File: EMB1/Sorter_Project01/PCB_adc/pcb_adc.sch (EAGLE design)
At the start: 10 parts, among them IC1 LM358N, K2 61201021621

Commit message: new boards
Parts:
- removed BLUE1, BLUE2, GREEN1, GREEN2, OPTO, RED1, RED2: (no value), led:LED5MM
- removed IC1: LM358N, linear:LM358N
- removed K2: 61201021621, Wurth_Elektronik_Electromechanic_Wire_to_Board_Connectors_rev15c:61201021621
- added K1: 61201021621, Wurth_Elektronik_Electromechanic_Wire_to_Board_Connectors_rev15c:61201021621
- added Q1, Q2, Q3: IRF512, transistor-power:IRF512
- added R2, R3, R8, R9: 1K, resistor:R-US_0204/7
- added R4, R5, R6: 100K, resistor:R-US_0204/7
- added R7: 430, resistor:R-US_0204/7
- added SL1: (no value), con-amp-quick:M12
- added U$1: MCP3008P, MCP3008:MCP3008P
- R1: value (none) -> 1K; device resistor:R-EU_0207/10 -> resistor:R-US_0204/7
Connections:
- removed net 12V: BLUE1.A, BLUE2.A, GREEN1.A, GREEN2.A, K2.1, RED1.A, RED2.A
- removed net 5V: IC1P.V+, K2.10
- removed net BLUE: BLUE1.C, BLUE2.C, K2.5
- removed net GREEN: GREEN1.C, GREEN2.C, K2.3
- removed net PHD: IC1A.OUT, K2.8, R1.2
- removed net RED: K2.7, RED1.C, RED2.C
- new net +12V: K1.1, SL1.12
- new net +5V: K1.10, SL1.9, U$1.VDD, U$1.VREF
- new net CLK: SL1.7, U$1.SCK
- new net CS: SL1.4, U$1.!CS
- new net C_BLUE: R3.1, SL1.1
- new net C_GREEN: R2.1, SL1.3
- new net C_RED: R1.1, SL1.2
- new net MISO: SL1.6, U$1.MISO
- new net MOSI: SL1.5, U$1.MOSI
- new net N$1: Q1.G, R1.2, R4.2
- new net N$3: Q3.G, R3.2, R6.2
- new net N$4: Q1.D, R7.1
- new net N$5: Q2.D, R8.1
- new net N$8: Q3.D, R9.1
- new net OPTO: K1.8, U$1.CH0
- new net V_BLUE: K1.5, R9.2
- new net V_GREEN: K1.3, R8.2
- new net V_RED: K1.7, R7.2
- net GND: now also K1.2, K1.4, K1.6, K1.9, Q1.S, Q2.S, Q3.S, R4.1, R5.1, R6.1, SL1.10, SL1.11, SL1.8, U$1.AGND, U$1.CH1, U$1.CH2, U$1.CH3, U$1.CH4, U$1.CH5, U$1.CH6, U$1.CH7, U$1.GND; no longer IC1A.-IN, IC1B.+IN, IC1B.-IN, IC1B.OUT, IC1P.V-, K2.2, K2.4, K2.6, K2.9, OPTO.A
- net N$2: now also Q2.G, R2.2, R5.2; no longer IC1A.+IN, OPTO.C, R1.1

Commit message: report images added
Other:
- moved on the sheet: K1, Q1, Q2, Q3, R1, R2, R3, R4, R5, R6, R7, R8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

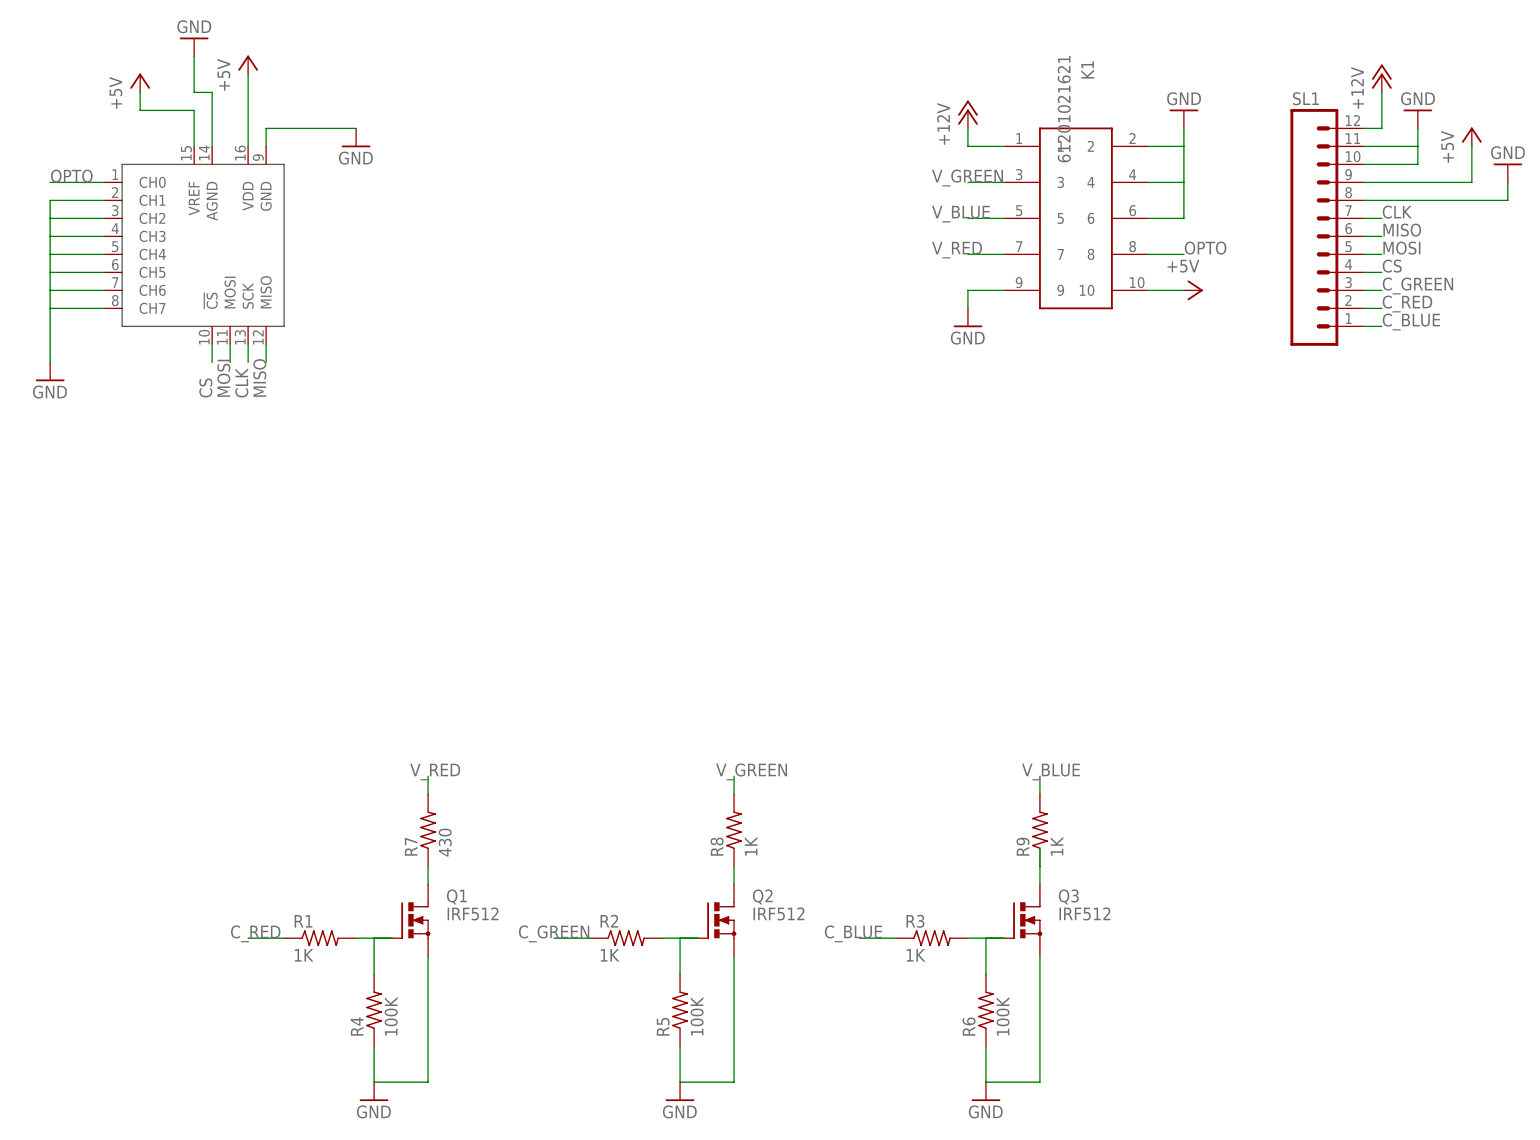
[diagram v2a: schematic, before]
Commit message: VHDL updated, now the blinking works due to bug pulsing data-updated for too long
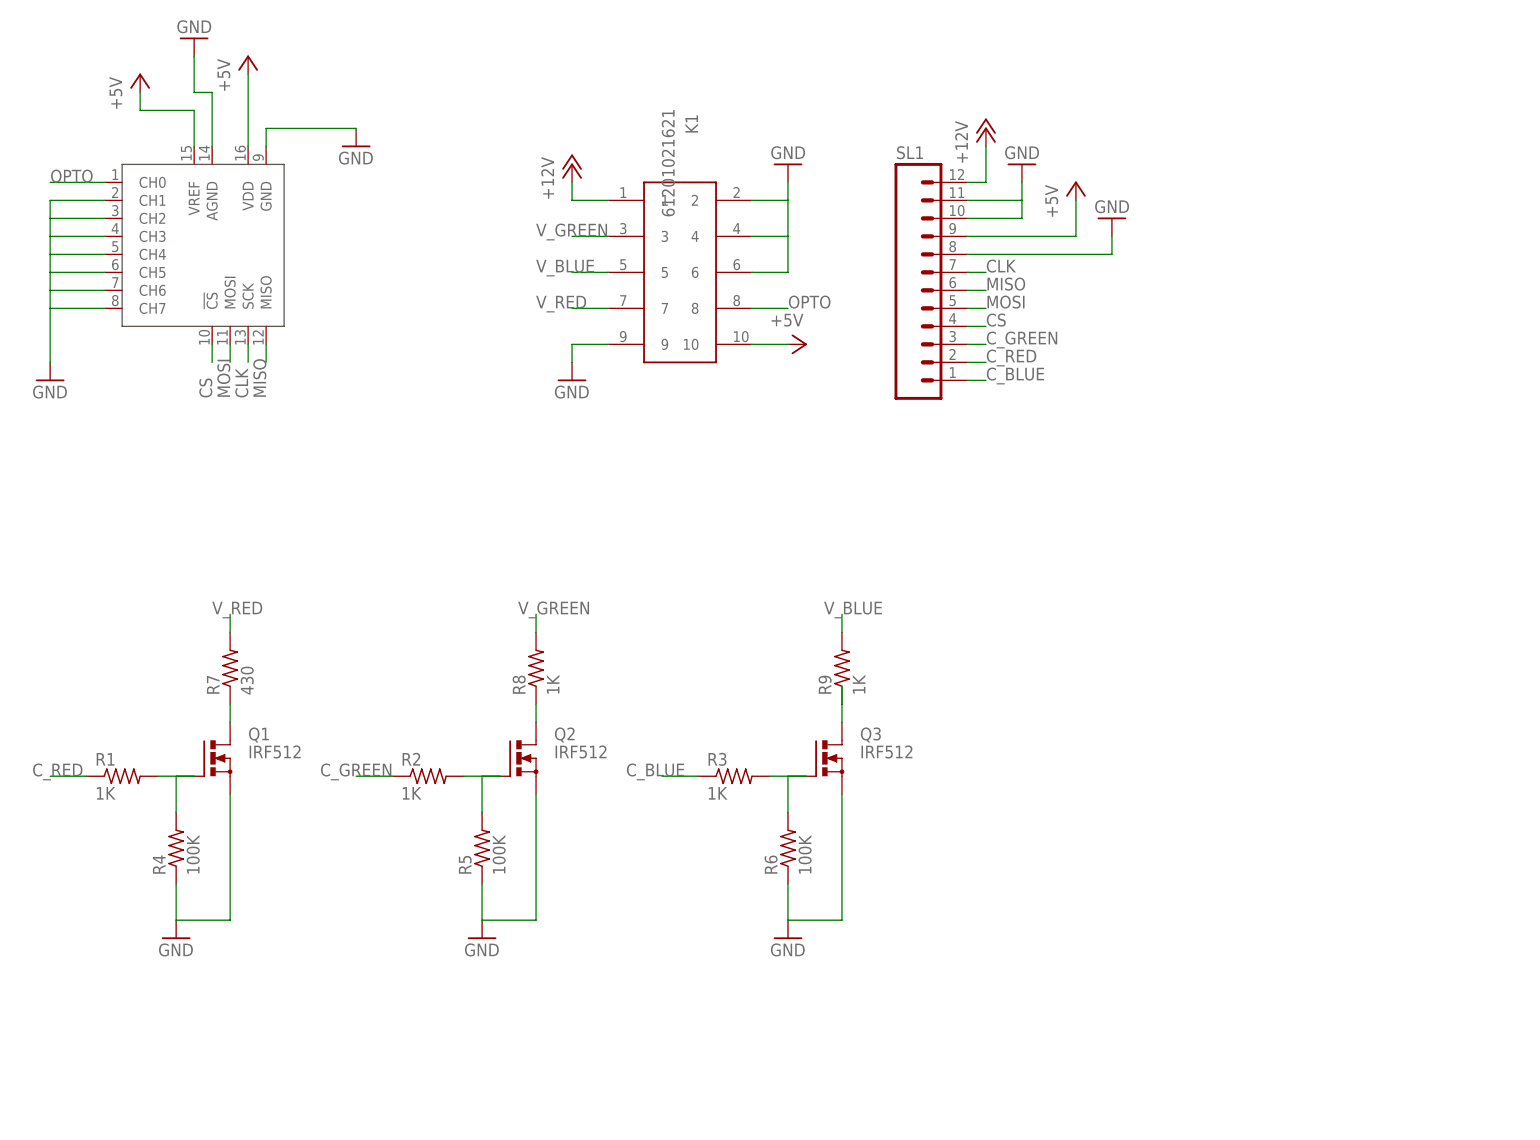
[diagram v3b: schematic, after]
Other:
- moved on the sheet: K1, Q1, Q2, Q3, R1, R2, R3, R4, R5, R6, R7, R8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

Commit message: report updated
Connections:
- new net +3V3: SL1.9, U$1.VDD, U$1.VREF
- net +5V: no longer SL1.9, U$1.VDD, U$1.VREF
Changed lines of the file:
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@@
 <part name="GND5" library="supply1" deviceset="GND" device=""/>
 <part name="GND6" library="supply1" deviceset="GND" device=""/>
-<part name="P+1" library="supply1" deviceset="+5V" device=""/>
-<part name="P+2" library="supply1" deviceset="+5V" device=""/>
 <part name="P+3" library="supply1" deviceset="+5V" device=""/>
 <part name="GND8" library="supply1" deviceset="GND" device=""/>
@@
 <part name="R8" library="resistor" deviceset="R-US_" device="0204/7" value="1K"/>
 <part name="R9" library="resistor" deviceset="R-US_" device="0204/7" value="1K"/>
-<part name="P+4" library="supply1" deviceset="+5V" device=""/>
 <part name="P+5" library="supply1" deviceset="+12V" device=""/>
 <part name="GND9" library="supply1" deviceset="GND" device=""/>
@@
 <part name="GND11" library="supply1" deviceset="GND" device=""/>
 <part name="P+7" library="supply1" deviceset="+12V" device=""/>
+<part name="+3V1" library="supply1" deviceset="+3V3" device=""/>
+<part name="+3V2" library="supply1" deviceset="+3V3" device=""/>
+<part name="+3V3" library="supply1" deviceset="+3V3" device=""/>
+<part name="+3V4" library="supply1" deviceset="+3V3" device=""/>
 </parts>
 <sheets>
@@
 <instance part="GND5" gate="1" x="7.62" y="99.06"/>
 <instance part="GND6" gate="1" x="38.1" y="66.04"/>
-<instance part="P+1" gate="1" x="-22.86" y="109.22"/>
-<instance part="P+2" gate="1" x="-7.62" y="111.76"/>
 <instance part="P+3" gate="1" x="71.12" y="71.12" rot="R270"/>
 <instance part="GND8" gate="1" x="-15.24" y="114.3" rot="R180"/>
@@
 <instance part="R8" gate="G$1" x="33.02" y="25.4" rot="R90"/>
 <instance part="R9" gate="G$1" x="76.2" y="25.4" rot="R90"/>
-<instance part="P+4" gate="1" x="109.22" y="93.98"/>
 <instance part="P+5" gate="1" x="96.52" y="101.6"/>
 <instance part="GND9" gate="1" x="114.3" y="88.9" rot="R180"/>
@@
 <instance part="GND11" gate="1" x="68.58" y="96.52" rot="R180"/>
 <instance part="P+7" gate="1" x="38.1" y="96.52"/>
+<instance part="+3V1" gate="G$1" x="-7.62" y="111.76"/>
+<instance part="+3V2" gate="G$1" x="-22.86" y="109.22"/>
+<instance part="+3V3" gate="G$1" x="76.2" y="73.66"/>
+<instance part="+3V4" gate="G$1" x="109.22" y="93.98"/>
 </instances>
 <busses>
@@
 <net name="+5V" class="0">
 <segment>
-<pinref part="U$1" gate="G$1" pin="VREF"/>
-<wire x1="-15.24" y1="99.06" x2="-15.24" y2="104.14" width="0.1524" layer="91"/>
-<wire x1="-15.24" y1="104.14" x2="-22.86" y2="104.14" width="0.1524" layer="91"/>
-<pinref part="P+1" gate="1" pin="+5V"/>
-<wire x1="-22.86" y1="104.14" x2="-22.86" y2="106.68" width="0.1524" layer="91"/>
-</segment>
-<segment>
-<pinref part="U$1" gate="G$1" pin="VDD"/>
-<pinref part="P+2" gate="1" pin="+5V"/>
-<wire x1="-7.62" y1="99.06" x2="-7.62" y2="109.22" width="0.1524" layer="91"/>
-</segment>
-<segment>
-<pinref part="P+4" gate="1" pin="+5V"/>
-<pinref part="SL1" gate="G$1" pin="9"/>
-<wire x1="93.98" y1="86.36" x2="109.22" y2="86.36" width="0.1524" layer="91"/>
-<wire x1="109.22" y1="86.36" x2="109.22" y2="91.44" width="0.1524" layer="91"/>
-</segment>
-<segment>
 <pinref part="K1" gate="G$1" pin="10"/>
 <pinref part="P+3" gate="1" pin="+5V"/>
@@
 </segment>
 </net>
+<net name="+3V3" class="0">
+<segment>
+<pinref part="U$1" gate="G$1" pin="VREF"/>
+<wire x1="-15.24" y1="99.06" x2="-15.24" y2="104.14" width="0.1524" layer="91"/>
+<wire x1="-15.24" y1="104.14" x2="-22.86" y2="104.14" width="0.1524" layer="91"/>
+<wire x1="-22.86" y1="104.14" x2="-22.86" y2="106.68" width="0.1524" layer="91"/>
+<pinref part="+3V2" gate="G$1" pin="+3V3"/>
+</segment>
+<segment>
+<pinref part="U$1" gate="G$1" pin="VDD"/>
+<wire x1="-7.62" y1="99.06" x2="-7.62" y2="109.22" width="0.1524" layer="91"/>
+<pinref part="+3V1" gate="G$1" pin="+3V3"/>
+</segment>
+<segment>
+<pinref part="SL1" gate="G$1" pin="9"/>
+<wire x1="93.98" y1="86.36" x2="109.22" y2="86.36" width="0.1524" layer="91"/>
+<wire x1="109.22" y1="86.36" x2="109.22" y2="91.44" width="0.1524" layer="91"/>
+<pinref part="+3V4" gate="G$1" pin="+3V3"/>
+</segment>
+</net>
